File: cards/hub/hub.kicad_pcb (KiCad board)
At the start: 2 copper layers, 100 x 100 mm, 28 parts, among them J1 USB_B, J2 BUS, J3 BUS

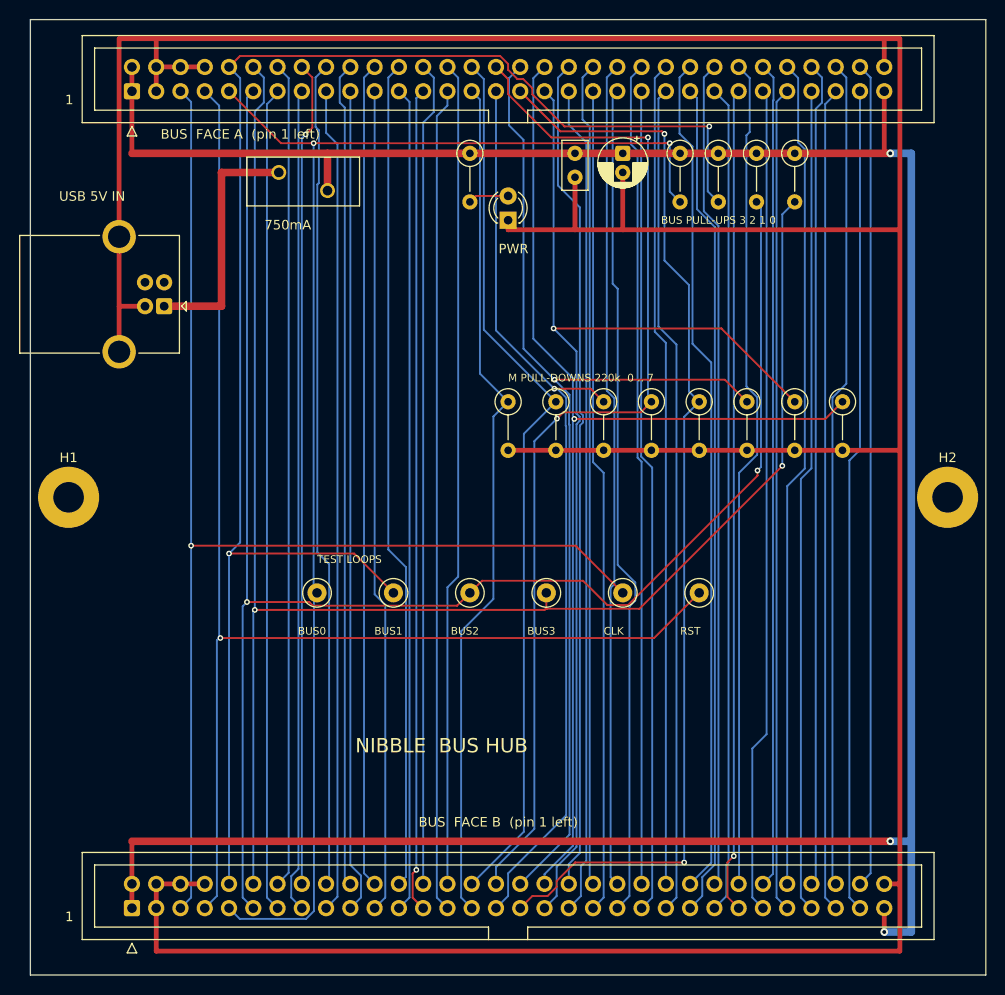
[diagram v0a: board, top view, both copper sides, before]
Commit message: Hub: bench-supply screw terminal and a 1.5 A polyfuse (D052)
The machine as built draws up to about 1.2 A (281 LEDs behind 1k, plus
the pull-ups), more than the 750 mA fuse and a computer's USB port were
ever going to carry. The hub now takes 5 V from a 5.08 mm screw terminal
on its left edge (the Kungber bench supply, 5.0 V with the limit at
1.5 A) as well as from the USB-B socket, both through a Bel 0ZRE0150FF
1.5 A polyfuse.

Routed with freerouting 2.4.1: 1.9 put an M5 via inside the 0.35 mm
bundle of the 64 bus lines and shorted M4/M5/M7 on two runs. KiCad DRC
and the JLCPCB-minimum DRC (0.127 track/space, 0.3/0.5 via, 0.5
hole-to-hole) both report no errors and nothing unconnected. Renders
checked. Parts table in order-1.md regenerated from bom.py (it had
also drifted from earlier card changes); bring-up, cards.md, README and
DECISIONS updated. The sim netlist is untouched (both parts are
sim=False), so the whole-machine proof stands.

Co-Authored-By: Claude Fable 5.1 <noreply@anthropic.com>
Claude-Session: https://claude.ai/code/session_01RktbhdQjDu7SpFpvkevyUU
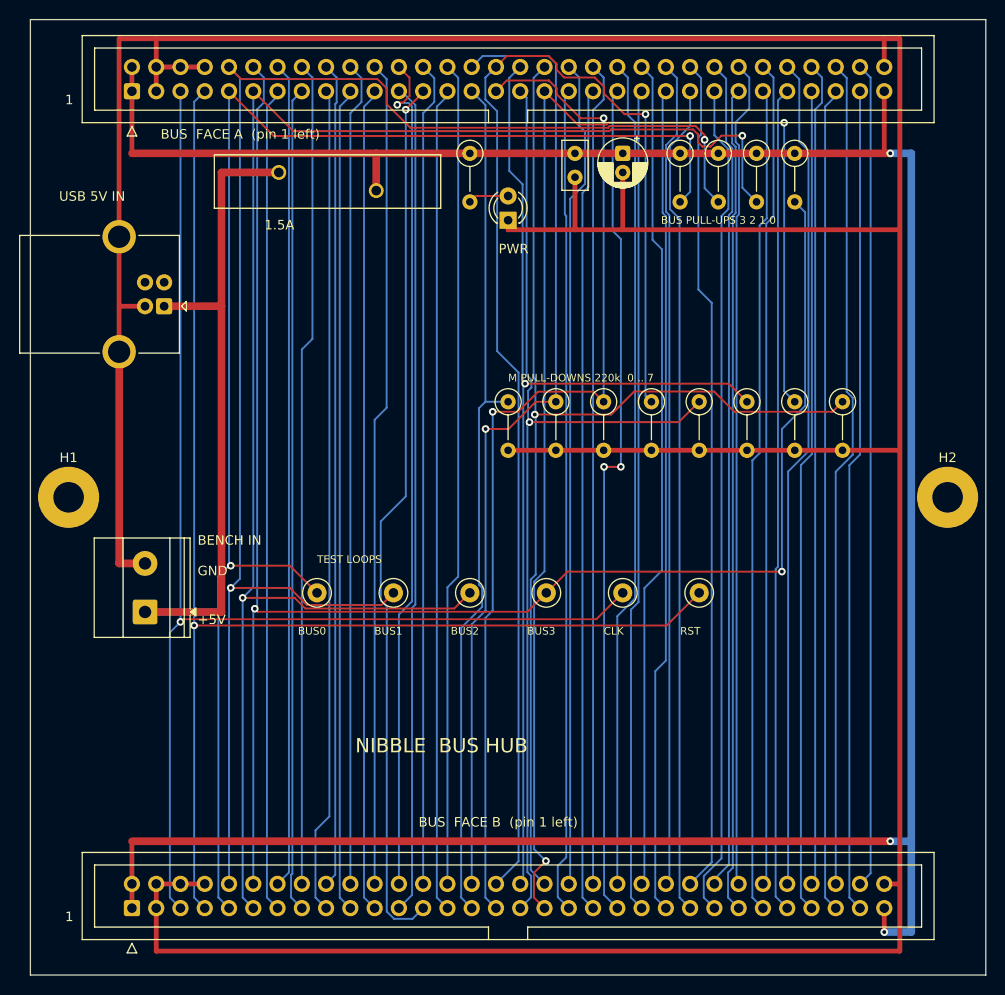
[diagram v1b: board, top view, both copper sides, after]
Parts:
- added J4: BUS, IDC-Header_2x32_P2.54mm_Vertical, F.Cu at (10.6, 93.0)
- F1: value 750mA -> 1.5A; footprint Fuse_BelFuse_0ZRE0075FF_L11.5mm_W4.8mm -> Fuse_BelFuse_0ZRE0150FF_L23.4mm_W5.3mm
- J2: value BUS -> BENCH 5V; footprint IDC-Header_2x32_P2.54mm_Vertical -> TerminalBlock_Phoenix_MKDS-1,5-2-5.08_1x02_P5.08mm_Horizontal
- moved J3 85.5 mm to (10.6, 7.50)
- moved J2 54.5 mm to (12.0, 62.0)
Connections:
- J2 pad 1: +5V -> VBUS
- J2 pad 2: +5V -> GND
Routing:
- net GND: track 412.3 -> 471.9 mm
- net VBUS: track 26.0 -> 66.0 mm
- net M3: track 109.7 -> 138.2 mm, vias 2 -> 1
- net M6: track 117.0 -> 143.7 mm, vias 1 -> 2
- net M2: track 97.5 -> 109.1 mm, vias 1 -> 2
- net M4: track 114.9 -> 105.6 mm, vias 2 -> 1
- net BUS0#: track 145.3 -> 154.3 mm
- net +5V: track 276.4 -> 285.4 mm
- net M1: track 92.8 -> 101.8 mm, vias 0 -> 1
- net PC4: track 86.4 -> 92.5 mm
- net BUS3#: track 177.7 -> 183.6 mm
- net M7: track 117.9 -> 121.5 mm
- net BUS2#: track 176.8 -> 173.6 mm
- net BUS1#: track 168.3 -> 166.2 mm
- net PC3: track 87.0 -> 88.9 mm, vias 0 -> 1
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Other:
- board text added: "+5V"
- board text added: "1.5A"
- board text added: "BENCH IN"
- board text added: "GND"
- board text removed: "750mA"

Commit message: Hub: the USB socket is gone (D057), the bench terminal is the only power entry
The machine is powered from the bench supply and nothing else, decided
with the pilot order on 2026-09-14; a socket nobody will plug in was a
part to buy, solder and explain, and a second path into the +5V rail.
The screw terminal moves up into the socket's place at the left edge,
its VBUS run to the 1.5 A polyfuse and its ground to the ring pre-routed
as before (the ground run past the top header's pin 1 at 0.5 mm: at
0.8 it broke the 0.15 mm clearance). The face-A silk label sits above
the terminal, clear of the fuse's body it used to run under. ERC 0,
freerouting 2.4.1 in one pass, DRC 0 errors, 0 open, clean under
JLCPCB's minimum rules.

Docs: DECISIONS D057 (supersedes the USB half of D052 and D015, the plug
as the switch); bring-up.md section 2 and the tools list without the
USB; cards/README.md, cards.md; order-1.md parts tables regenerated
(pilot 319, machine 7128).

Co-Authored-By: Claude Fable 5.1 <noreply@anthropic.com>
Claude-Session: https://claude.ai/code/session_01RktbhdQjDu7SpFpvkevyUU
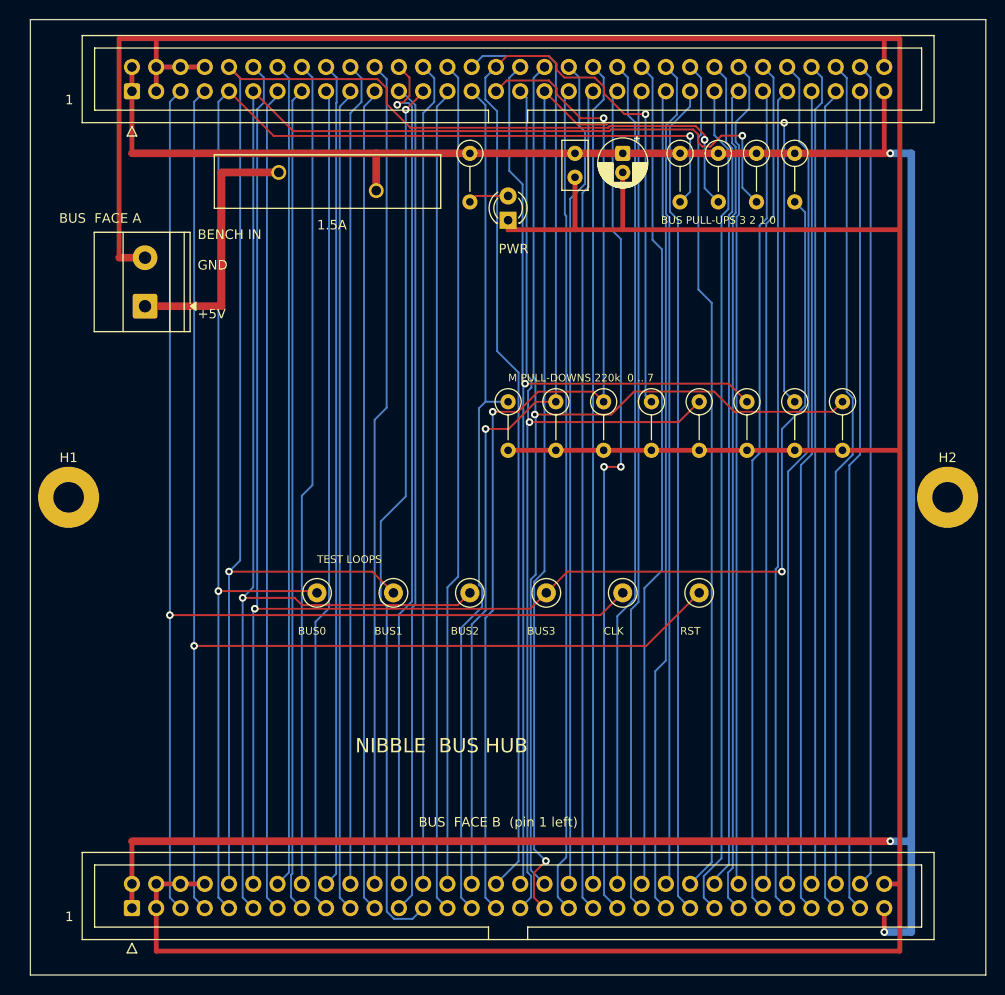
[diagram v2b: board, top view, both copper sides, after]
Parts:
- removed J4: BUS, IDC-Header_2x32_P2.54mm_Vertical
- J1: value USB_B -> BENCH 5V; footprint USB_B_OST_USB-B1HSxx_Horizontal -> TerminalBlock_Phoenix_MKDS-1,5-2-5.08_1x02_P5.08mm_Horizontal
- J2: value BENCH 5V -> BUS; footprint TerminalBlock_Phoenix_MKDS-1,5-2-5.08_1x02_P5.08mm_Horizontal -> IDC-Header_2x32_P2.54mm_Vertical
- moved J3 85.5 mm to (10.6, 93.0)
- moved J2 54.5 mm to (10.6, 7.50)
- moved J1 2.00 mm to (12.0, 30.0), turned to 90 degrees
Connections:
- J1 pad 2: unconnected-(J1-D--Pad2) -> GND
- J2 pad 1: VBUS -> +5V
- J2 pad 2: GND -> +5V
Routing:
- net GND: track 471.9 -> 422.5 mm
- net VBUS: track 66.0 -> 28.0 mm
- net RST: track 140.7 -> 141.6 mm
- net CLK: track 134.0 -> 134.8 mm
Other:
- board text added: "BUS FACE A"
- board text removed: "BUS FACE A (pin 1 left)"
- board text removed: "USB 5V IN"

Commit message: Hub: two 4 mm banana sockets for the bench supply (D058)
Bench supplies speak 4 mm banana: the leads plug in, polarity is the
colour, nothing is bare or screwed. The sockets stand on the hub's front
face (red +5V above black GND, 19.05 mm apart so a dual plug fits too)
because the card's edges are not reachable in the frame, 10 mm from the
next card and from the upright; edge-entry sockets, barrel jacks and XT
connectors all want a free edge. KiCad's Banana_Jack_1Pin footprint, a
6.1 mm plated hole for a panel-type socket (Cliff S16, Hirschmann BIL 20
or any red/black pair). The red socket's run to the 1.5 A polyfuse and
the black one's run up the left edge to the ground ring are pre-routed;
ERC 0, freerouting 2.4.1 in one pass, DRC 0 errors, 0 open, clean under
JLCPCB's minimum rules. Replaces the screw terminal of D057.

bom.py names the socket; order-1.md tables regenerated (pilot 320,
machine 7129); bring-up.md, cards/README.md, cards.md; DECISIONS D058.

Co-Authored-By: Claude Fable 5.1 <noreply@anthropic.com>
Claude-Session: https://claude.ai/code/session_01RktbhdQjDu7SpFpvkevyUU
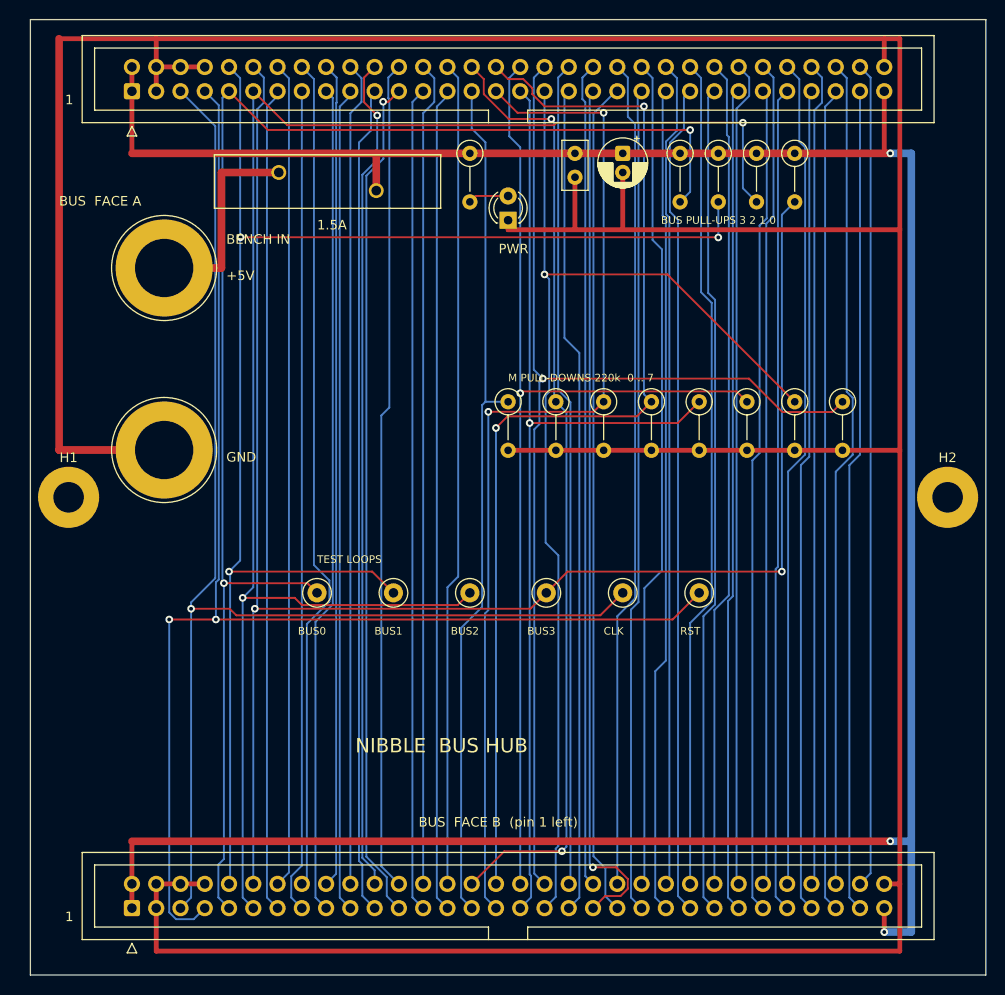
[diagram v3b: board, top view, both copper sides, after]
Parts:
- added J4: BUS, IDC-Header_2x32_P2.54mm_Vertical, F.Cu at (10.6, 93.0)
- J1: value BENCH 5V -> BENCH +5V; footprint TerminalBlock_Phoenix_MKDS-1,5-2-5.08_1x02_P5.08mm_Horizontal -> Banana_Jack_1Pin
- J2: value BUS -> BENCH GND; footprint IDC-Header_2x32_P2.54mm_Vertical -> Banana_Jack_1Pin
- moved J3 85.5 mm to (10.6, 7.50)
- moved J2 37.7 mm to (14.0, 45.0), turned to 0 degrees
- moved J1 4.47 mm to (14.0, 26.0), turned to 0 degrees
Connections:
- J2 pad 1: +5V -> GND
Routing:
- net GND: track 422.5 -> 467.2 mm
- net M6: track 143.7 -> 118.7 mm, vias 2 -> 1
- net M3: track 138.2 -> 113.9 mm, vias 1 -> 2
- net BUS1#: track 166.0 -> 158.5 mm, vias 2 -> 3
- net RST: track 141.6 -> 147.8 mm, vias 1 -> 2
- net PC4: track 92.5 -> 86.4 mm, vias 1 -> 0
- net VBUS: track 28.0 -> 22.0 mm
- net SUB: track 86.4 -> 91.2 mm, vias 0 -> 1
- net M1: track 101.8 -> 99.9 mm, vias 1 -> 2
- net PC3: track 88.9 -> 87.1 mm, vias 1 -> 0
- net PC2: track 87.1 -> 88.7 mm, vias 0 -> 1
- net M2: track 109.1 -> 107.5 mm
- net A3: track 86.4 -> 87.9 mm
- net PC1: track 86.5 -> 87.7 mm, vias 0 -> 1
- net M7: track 121.5 -> 120.4 mm
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
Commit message: Hub: the bus lines leave the banana sockets' nuts alone; the order gate checks what the hardware touches
The first hub route had CLK 0.17 mm from the +5V socket's copper ring and RST
and BUS0# within 6 mm of both sockets' centres, on the back, where the socket's
M6 nut and solder tag clamp onto the ring: 25 um of solder mask between the
clock and the supply. DRC at 0.15 mm was content. Found when the renders were
questioned (why do the sockets look like bare holes: because they are, the
footprint is a 6.1 mm hole in a 10.16 mm ring and the nut is the connection),
not by the audit that preceded it.

The hub's plan now fences a 15 mm square around each socket on both faces
(router keep-outs, as the sequencer's matrix has). CLK and RST leave the top
header from the columns right above the sockets and the router gave them up
behind the fence, so they are led by hand on the back: off the pin, left below
the header, down the free strip at the card's edge, right between the two
sockets, to a hand-off via the router wires on. pcb.py drops a hand-off via
again when the router stays on the same layer (a plan via with a fourth field
True; the pour cards' one-layer vias meet the pour and are not touched).
Routed clean on the first attempt: 0 unconnected, 0 DRC items.

order_check.py gets a clamp check: no copper of another net within 7.5 mm of a
banana socket's centre (an M6 nut's corners and a 12 mm tag reach 6.4 mm) or
3.3 mm of a mounting hole's (a hex standoff's corners, no washers), either
face, pad positions turned by the footprint's angle. It flags the six tracks
of the previous hub (b5708fb) and passes all 25 boards as they stand.
order-1.md section 5 lists the failure classes no tool measures, so the list
can be argued with; the socket spec names the M6 panel type (Hirschmann BIL 20)
and drops the Cliff S16, a shrouded safety socket on a 10.8 mm cutout.
mounting.md: no washers on the M3 screws.

Co-Authored-By: Claude Fable 5.1 <noreply@anthropic.com>
Claude-Session: h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
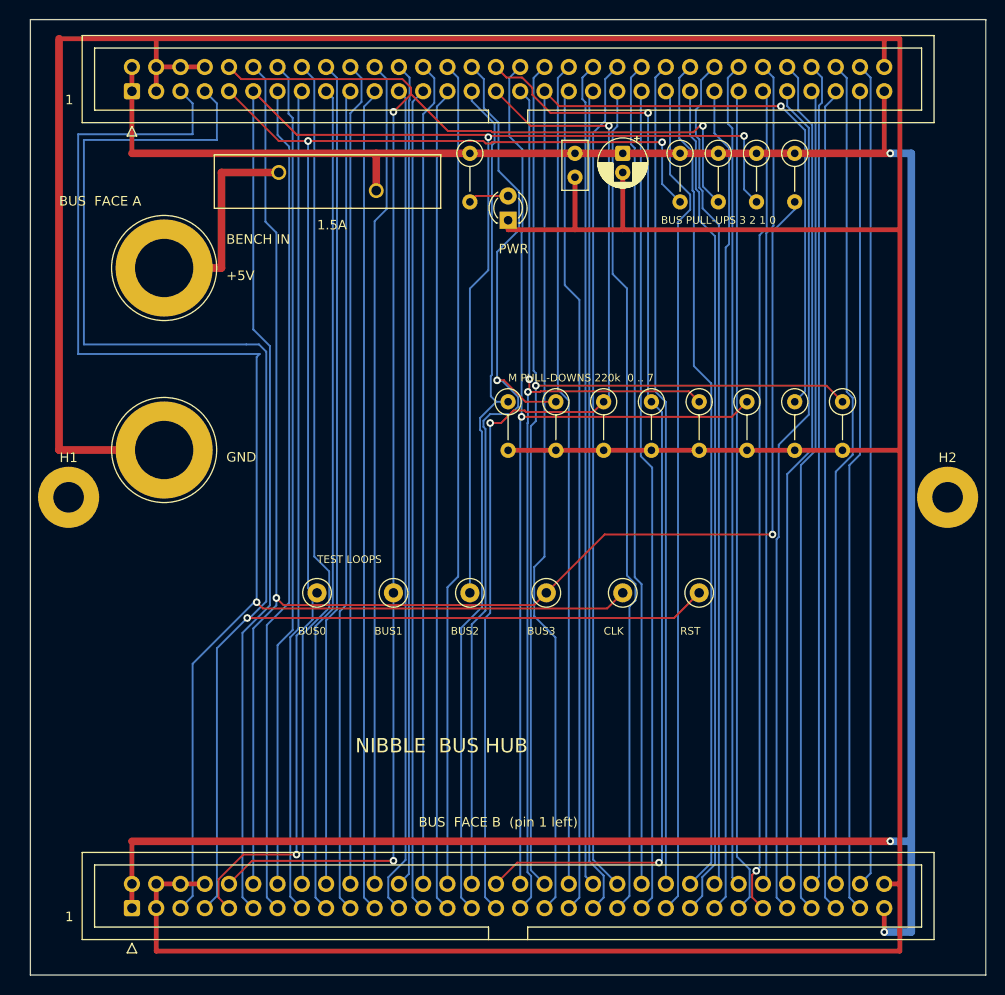
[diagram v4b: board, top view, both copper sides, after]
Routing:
- net M6: track 118.7 -> 145.2 mm
- net CLK: track 135.0 -> 159.9 mm
- net BUS2#: track 172.8 -> 197.3 mm
- net RST: track 147.8 -> 169.8 mm, vias 2 -> 1
- net BUS0#: track 154.6 -> 143.4 mm, vias 2 -> 3
- net GND: track 467.2 -> 457.2 mm
- net SUB: track 91.2 -> 86.7 mm, vias 1 -> 0
- net BUS3#: track 182.4 -> 178.6 mm
- net BUS1#: track 158.5 -> 160.9 mm
- net MI: track 86.5 -> 88.3 mm
- net PC2: track 88.7 -> 87.0 mm, vias 1 -> 0
- net M3: track 113.9 -> 115.5 mm
- net PC1: track 87.7 -> 86.5 mm, vias 1 -> 0
- net A0: track 86.4 -> 87.4 mm
- net BA: track 86.7 -> 87.6 mm
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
